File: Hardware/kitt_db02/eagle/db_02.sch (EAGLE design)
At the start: 30 parts, among them T8.1 TPTP09SQ, T8.2 TPTP09SQ, U8 MCP23017ML, X8.1 CON_HEADER_1X08-SMD

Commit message: finished bill of materials for db02 -> layout needs a bit more work on the connector,    which now feature gnd and v+
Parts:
- added J1: FTS-109-01-L-DV, kitt.con:FTS-109-01-L-DV
- renumbered U8 to U8.0
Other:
- note added: "remove"
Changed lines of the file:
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@@
 </classes>
 <parts>
-<part name="U8" library="microchip" deviceset="MCP23017" device="ML" value="MCP23017ML"/>
+<part name="U8.0" library="microchip" deviceset="MCP23017" device="ML" value="MCP23017ML"/>
 <part name="D8.0" library="led" deviceset="LED" device="CHIPLED_1206"/>
 <part name="D8.1" library="led" deviceset="LED" device="CHIPLED_1206"/>
@@
 <part name="GND4" library="supply1" deviceset="GND" device=""/>
 <part name="P+6" library="supply1" deviceset="V+" device=""/>
+<part name="J1" library="kitt.con" deviceset="FTS-109-01-L-DV" device=""/>
 </parts>
 <sheets>
 <sheet>
 <plain>
+<text x="139.7" y="27.94" size="6.4516" layer="98" rot="R180">remove</text>
 </plain>
 <instances>
-<instance part="U8" gate="G$1" x="27.94" y="35.56"/>
+<instance part="U8.0" gate="G$1" x="27.94" y="35.56"/>
 <instance part="D8.0" gate="G$1" x="50.8" y="66.04" rot="MR0"/>
 <instance part="D8.1" gate="G$1" x="60.96" y="66.04" rot="MR0"/>
@@
 <instance part="GND4" gate="1" x="15.24" y="81.28"/>
 <instance part="P+6" gate="1" x="15.24" y="114.3"/>
+<instance part="J1" gate="A" x="149.86" y="25.4"/>
 </instances>
 <busses>
@@
 <net name="N$1" class="0">
 <segment>
-<pinref part="U8" gate="G$1" pin="GPA0"/>
+<pinref part="U8.0" gate="G$1" pin="GPA0"/>
 <pinref part="D8.0" gate="G$1" pin="C"/>
 <wire x1="40.64" y1="55.88" x2="50.8" y2="55.88" width="0.1524" layer="91"/>
@@
 <net name="N$2" class="0">
 <segment>
-<pinref part="U8" gate="G$1" pin="GPA1"/>
+<pinref part="U8.0" gate="G$1" pin="GPA1"/>
 <pinref part="D8.1" gate="G$1" pin="C"/>
 <wire x1="40.64" y1="53.34" x2="60.96" y2="53.34" width="0.1524" layer="91"/>
@@
 <net name="N$3" class="0">
 <segment>
-<pinref part="U8" gate="G$1" pin="GPA2"/>
+<pinref part="U8.0" gate="G$1" pin="GPA2"/>
 <pinref part="D8.2" gate="G$1" pin="C"/>
 <wire x1="40.64" y1="50.8" x2="71.12" y2="50.8" width="0.1524" layer="91"/>
@@
 <net name="N$4" class="0">
 <segment>
-<pinref part="U8" gate="G$1" pin="GPA3"/>
+<pinref part="U8.0" gate="G$1" pin="GPA3"/>
 <pinref part="D8.3" gate="G$1" pin="C"/>
 <wire x1="40.64" y1="48.26" x2="81.28" y2="48.26" width="0.1524" layer="91"/>
@@
 <net name="N$5" class="0">
 <segment>
-<pinref part="U8" gate="G$1" pin="GPA4"/>
+<pinref part="U8.0" gate="G$1" pin="GPA4"/>
 <pinref part="D8.4" gate="G$1" pin="C"/>
 <wire x1="40.64" y1="45.72" x2="91.44" y2="45.72" width="0.1524" layer="91"/>
@@
 <net name="N$6" class="0">
 <segment>
-<pinref part="U8" gate="G$1" pin="GPA5"/>
+<pinref part="U8.0" gate="G$1" pin="GPA5"/>
 <pinref part="D8.5" gate="G$1" pin="C"/>
 <wire x1="40.64" y1="43.18" x2="101.6" y2="43.18" width="0.1524" layer="91"/>
@@
 <net name="N$7" class="0">
 <segment>
-<pinref part="U8" gate="G$1" pin="GPA6"/>
+<pinref part="U8.0" gate="G$1" pin="GPA6"/>
 <pinref part="D8.6" gate="G$1" pin="C"/>
 <wire x1="40.64" y1="40.64" x2="111.76" y2="40.64" width="0.1524" layer="91"/>
@@
 <net name="N$8" class="0">
 <segment>
-<pinref part="U8" gate="G$1" pin="GPA7"/>
+<pinref part="U8.0" gate="G$1" pin="GPA7"/>
 <pinref part="D8.7" gate="G$1" pin="C"/>
 <wire x1="40.64" y1="38.1" x2="121.92" y2="38.1" width="0.1524" layer="91"/>
@@
 <segment>
 <pinref part="P+1" gate="1" pin="V+"/>
-<pinref part="U8" gate="G$1" pin="VDD"/>
+<pinref part="U8.0" gate="G$1" pin="VDD"/>
 <wire x1="12.7" y1="58.42" x2="12.7" y2="55.88" width="0.1524" layer="91"/>
 <wire x1="12.7" y1="55.88" x2="15.24" y2="55.88" width="0.1524" layer="91"/>
@@
 <segment>
 <pinref part="P+5" gate="1" pin="V+"/>
-<pinref part="U8" gate="G$1" pin="!RESET"/>
+<pinref part="U8.0" gate="G$1" pin="!RESET"/>
 <wire x1="5.08" y1="58.42" x2="5.08" y2="50.8" width="0.1524" layer="91"/>
 <wire x1="5.08" y1="50.8" x2="15.24" y2="50.8" width="0.1524" layer="91"/>
@@
 <segment>
 <pinref part="GND2" gate="1" pin="GND"/>
-<pinref part="U8" gate="G$1" pin="VSS"/>
+<pinref part="U8.0" gate="G$1" pin="VSS"/>
 <wire x1="10.16" y1="10.16" x2="10.16" y2="15.24" width="0.1524" layer="91"/>
 <wire x1="10.16" y1="15.24" x2="15.24" y2="15.24" width="0.1524" layer="91"/>
@@
 <wire x1="15.24" y1="33.02" x2="5.08" y2="33.02" width="0.1524" layer="91"/>
 <label x="5.08" y="33.02" size="1.27" layer="95" rot="R180" xref="yes"/>
-<pinref part="U8" gate="G$1" pin="SCL"/>
+<pinref part="U8.0" gate="G$1" pin="SCL"/>
 </segment>
 <segment>
@@
 <wire x1="15.24" y1="30.48" x2="5.08" y2="30.48" width="0.1524" layer="91"/>
 <label x="5.08" y="30.48" size="1.27" layer="95" rot="R180" xref="yes"/>
-<pinref part="U8" gate="G$1" pin="SDA"/>
+<pinref part="U8.0" gate="G$1" pin="SDA"/>
 </segment>
 <segment>
@@
 <pinref part="R8.11" gate="G$1" pin="2"/>
 <wire x1="-15.24" y1="30.48" x2="-15.24" y2="25.4" width="0.1524" layer="91"/>
-<pinref part="U8" gate="G$1" pin="A0"/>
+<pinref part="U8.0" gate="G$1" pin="A0"/>
 <wire x1="-15.24" y1="25.4" x2="-15.24" y2="17.78" width="0.1524" layer="91"/>
 <wire x1="15.24" y1="25.4" x2="-15.24" y2="25.4" width="0.1524" layer="91"/>
@@
 <pinref part="R8.12" gate="G$1" pin="2"/>
 <wire x1="-25.4" y1="30.48" x2="-25.4" y2="22.86" width="0.1524" layer="91"/>
-<pinref part="U8" gate="G$1" pin="A1"/>
+<pinref part="U8.0" gate="G$1" pin="A1"/>
 <wire x1="-25.4" y1="22.86" x2="-25.4" y2="17.78" width="0.1524" layer="91"/>
 <wire x1="15.24" y1="22.86" x2="-25.4" y2="22.86" width="0.1524" layer="91"/>
@@
 <pinref part="R8.13" gate="G$1" pin="2"/>
 <wire x1="-35.56" y1="30.48" x2="-35.56" y2="20.32" width="0.1524" layer="91"/>
-<pinref part="U8" gate="G$1" pin="A2"/>
+<pinref part="U8.0" gate="G$1" pin="A2"/>
 <wire x1="-35.56" y1="20.32" x2="-35.56" y2="17.78" width="0.1524" layer="91"/>
 <wire x1="15.24" y1="20.32" x2="-35.56" y2="20.32" width="0.1524" layer="91"/>
@@
 <net name="GPB0" class="0">
 <segment>
-<pinref part="U8" gate="G$1" pin="GPB0"/>
+<pinref part="U8.0" gate="G$1" pin="GPB0"/>
 <wire x1="48.26" y1="33.02" x2="40.64" y2="33.02" width="0.1524" layer="91"/>
 <label x="43.18" y="33.02" size="1.27" layer="95"/>
@@
 <net name="GPB1" class="0">
 <segment>
-<pinref part="U8" gate="G$1" pin="GPB1"/>
+<pinref part="U8.0" gate="G$1" pin="GPB1"/>
 <wire x1="40.64" y1="30.48" x2="48.26" y2="30.48" width="0.1524" layer="91"/>
 <label x="43.18" y="30.48" size="1.27" layer="95"/>
@@
 </segment>
 <segment>
-<pinref part="U8" gate="G$1" pin="GPB2"/>
+<pinref part="U8.0" gate="G$1" pin="GPB2"/>
 <wire x1="40.64" y1="27.94" x2="48.26" y2="27.94" width="0.1524" layer="91"/>
 <label x="43.18" y="27.94" size="1.27" layer="95"/>
@@
 <net name="GPB3" class="0">
 <segment>
-<pinref part="U8" gate="G$1" pin="GPB3"/>
+<pinref part="U8.0" gate="G$1" pin="GPB3"/>
 <wire x1="48.26" y1="25.4" x2="40.64" y2="25.4" width="0.1524" layer="91"/>
 <label x="43.18" y="25.4" size="1.27" layer="95"/>
@@
 <net name="GPB4" class="0">
 <segment>
-<pinref part="U8" gate="G$1" pin="GPB4"/>
+<pinref part="U8.0" gate="G$1" pin="GPB4"/>
 <wire x1="40.64" y1="22.86" x2="48.26" y2="22.86" width="0.1524" layer="91"/>
 <label x="43.18" y="22.86" size="1.27" layer="95"/>
@@
 <net name="GPB5" class="0">
 <segment>
-<pinref part="U8" gate="G$1" pin="GPB5"/>
+<pinref part="U8.0" gate="G$1" pin="GPB5"/>
 <wire x1="40.64" y1="20.32" x2="48.26" y2="20.32" width="0.1524" layer="91"/>
 <label x="43.18" y="20.32" size="1.27" layer="95"/>
@@
 </segment>
 <segment>
-<pinref part="U8" gate="G$1" pin="GPB6"/>
+<pinref part="U8.0" gate="G$1" pin="GPB6"/>
 <wire x1="40.64" y1="17.78" x2="48.26" y2="17.78" width="0.1524" layer="91"/>
 <label x="43.18" y="17.78" size="1.27" layer="95"/>
@@
 </segment>
 <segment>
-<pinref part="U8" gate="G$1" pin="GPB7"/>
+<pinref part="U8.0" gate="G$1" pin="GPB7"/>
 <wire x1="40.64" y1="15.24" x2="48.26" y2="15.24" width="0.1524" layer="91"/>
 <label x="43.18" y="15.24" size="1.27" layer="95"/>
@@
 <segment>
 <pinref part="T8.1" gate="G$1" pin="TP"/>
-<pinref part="U8" gate="G$1" pin="INTA"/>
+<pinref part="U8.0" gate="G$1" pin="INTA"/>
 <wire x1="2.54" y1="45.72" x2="15.24" y2="45.72" width="0.1524" layer="91"/>
 </segment>
@@
 <segment>
 <pinref part="T8.2" gate="G$1" pin="TP"/>
-<pinref part="U8" gate="G$1" pin="INTB"/>
+<pinref part="U8.0" gate="G$1" pin="INTB"/>
 <wire x1="-2.54" y1="43.18" x2="15.24" y2="43.18" width="0.1524" layer="91"/>
 </segment>

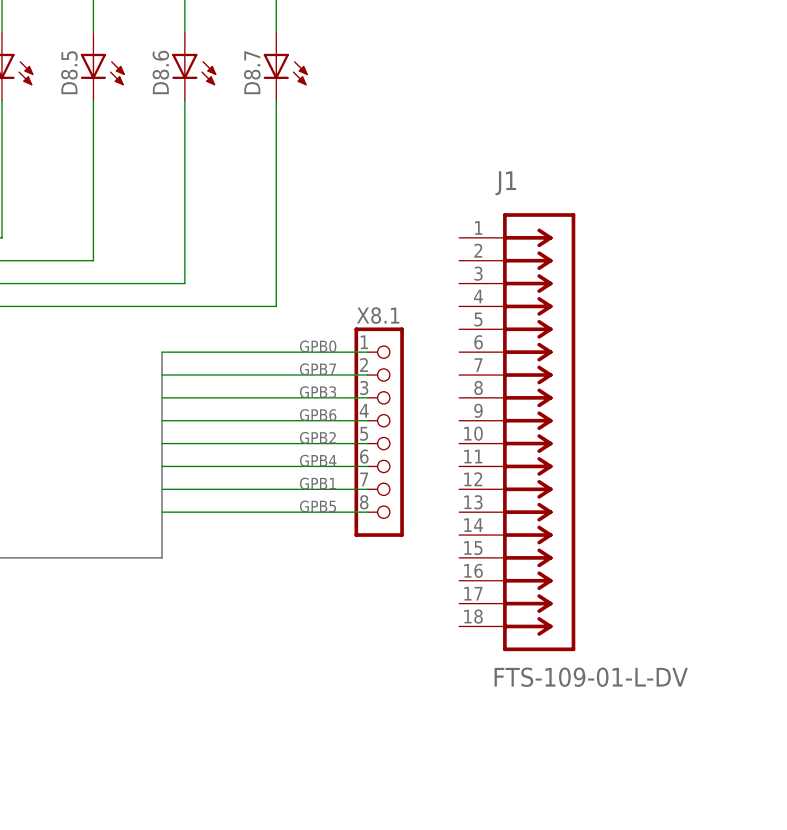
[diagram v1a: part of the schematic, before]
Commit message: snapshot of db02 board layout : this is going nowhere edition -> reverting back to previous version
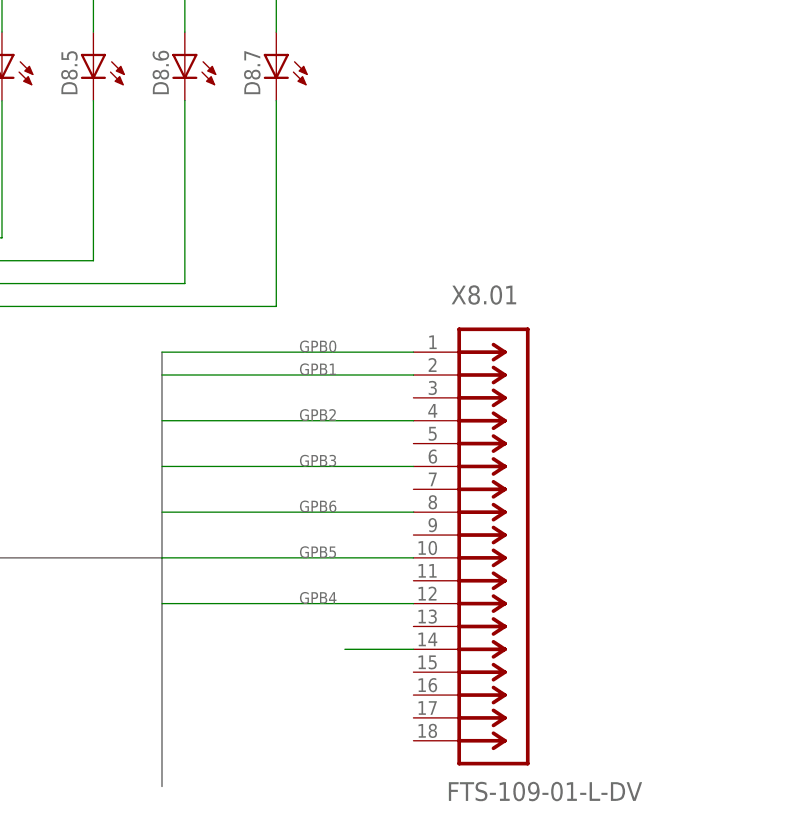
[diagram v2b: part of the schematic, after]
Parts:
- removed J1: FTS-109-01-L-DV, kitt.con:FTS-109-01-L-DV
- removed X8.1: CON_HEADER_1X08-SMD, dp_devices:CON_HEADER_1X08-SMD
- added X8.01: FTS-109-01-L-DV, kitt.con:FTS-109-01-L-DV
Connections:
- net GPB0: now also X8.01.1; no longer X8.1.1
- net GPB1: now also X8.01.2; no longer X8.1.7
- net GPB2: now also X8.01.4; no longer X8.1.5
- net GPB3: now also X8.01.6; no longer X8.1.3
- net GPB4: now also X8.01.12; no longer X8.1.6
- net GPB5: now also X8.01.10; no longer X8.1.8
- net GPB6: now also X8.01.8; no longer X8.1.4
- net GPB7: now also X8.01.14; no longer X8.1.2
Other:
- note removed: "remove"
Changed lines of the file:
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@@
 <part name="GND3" library="supply1" deviceset="GND" device=""/>
 <part name="P+5" library="supply1" deviceset="V+" device=""/>
-<part name="X8.1" library="dp_devices" deviceset="CON_HEADER_1X08" device="-SMD"/>
 <part name="T8.1" library="testpad" deviceset="TP" device="TP09SQ" value="TPTP09SQ"/>
 <part name="T8.2" library="testpad" deviceset="TP" device="TP09SQ" value="TPTP09SQ"/>
@@
 <part name="GND4" library="supply1" deviceset="GND" device=""/>
 <part name="P+6" library="supply1" deviceset="V+" device=""/>
-<part name="J1" library="kitt.con" deviceset="FTS-109-01-L-DV" device=""/>
+<part name="X8.01" library="kitt.con" deviceset="FTS-109-01-L-DV" device=""/>
 </parts>
 <sheets>
 <sheet>
 <plain>
-<text x="139.7" y="27.94" size="6.4516" layer="98" rot="R180">remove</text>
 </plain>
 <instances>
@@
 <instance part="GND3" gate="1" x="-25.4" y="0"/>
 <instance part="P+5" gate="1" x="5.08" y="60.96"/>
-<instance part="X8.1" gate="J" x="132.08" y="25.4"/>
 <instance part="T8.1" gate="G$1" x="0" y="45.72" rot="R90"/>
 <instance part="T8.2" gate="G$1" x="-5.08" y="43.18" rot="R90"/>
@@
 <instance part="GND4" gate="1" x="15.24" y="81.28"/>
 <instance part="P+6" gate="1" x="15.24" y="114.3"/>
-<instance part="J1" gate="A" x="149.86" y="25.4"/>
+<instance part="X8.01" gate="A" x="144.78" y="12.7"/>
 </instances>
 <busses>
@@
 <wire x1="48.26" y1="10.16" x2="109.22" y2="10.16" width="0.762" layer="92"/>
 <wire x1="109.22" y1="10.16" x2="109.22" y2="33.02" width="0.762" layer="92"/>
+<wire x1="109.22" y1="10.16" x2="109.22" y2="-15.24" width="0.762" layer="92"/>
 </segment>
 </bus>
@@
 </segment>
 <segment>
-<pinref part="X8.1" gate="J" pin="1"/>
-<wire x1="132.08" y1="33.02" x2="109.22" y2="33.02" width="0.1524" layer="91"/>
 <label x="124.46" y="33.02" size="1.27" layer="95"/>
+<pinref part="X8.01" gate="A" pin="1"/>
+<wire x1="137.16" y1="33.02" x2="109.22" y2="33.02" width="0.1524" layer="91"/>
 </segment>
 </net>
@@
 </segment>
 <segment>
-<pinref part="X8.1" gate="J" pin="7"/>
-<wire x1="109.22" y1="17.78" x2="132.08" y2="17.78" width="0.1524" layer="91"/>
-<label x="124.46" y="17.78" size="1.27" layer="95"/>
+<pinref part="X8.01" gate="A" pin="2"/>
+<wire x1="109.22" y1="30.48" x2="137.16" y2="30.48" width="0.1524" layer="91"/>
+<label x="124.46" y="30.48" size="1.27" layer="95"/>
 </segment>
 </net>
 <net name="GPB2" class="0">
-<segment>
-<pinref part="X8.1" gate="J" pin="5"/>
-<wire x1="109.22" y1="22.86" x2="132.08" y2="22.86" width="0.1524" layer="91"/>
-<label x="124.46" y="22.86" size="1.27" layer="95"/>
-</segment>
 <segment>
 <pinref part="U8.0" gate="G$1" pin="GPB2"/>
@@
 <label x="43.18" y="27.94" size="1.27" layer="95"/>
 </segment>
+<segment>
+<wire x1="109.22" y1="25.4" x2="137.16" y2="25.4" width="0.1524" layer="91"/>
+<label x="124.46" y="25.4" size="1.27" layer="95"/>
+<pinref part="X8.01" gate="A" pin="4"/>
+</segment>
 </net>
 <net name="GPB3" class="0">
@@
 </segment>
 <segment>
-<pinref part="X8.1" gate="J" pin="3"/>
-<wire x1="132.08" y1="27.94" x2="109.22" y2="27.94" width="0.1524" layer="91"/>
-<label x="124.46" y="27.94" size="1.27" layer="95"/>
+<pinref part="X8.01" gate="A" pin="6"/>
+<wire x1="109.22" y1="20.32" x2="137.16" y2="20.32" width="0.1524" layer="91"/>
+<label x="124.46" y="20.32" size="1.27" layer="95"/>
 </segment>
 </net>
@@
 </segment>
 <segment>
-<pinref part="X8.1" gate="J" pin="6"/>
-<wire x1="109.22" y1="20.32" x2="132.08" y2="20.32" width="0.1524" layer="91"/>
-<label x="124.46" y="20.32" size="1.27" layer="95"/>
+<wire x1="109.22" y1="5.08" x2="137.16" y2="5.08" width="0.1524" layer="91"/>
+<label x="124.46" y="5.08" size="1.27" layer="95"/>
+<pinref part="X8.01" gate="A" pin="12"/>
 </segment>
 </net>
@@
 </segment>
 <segment>
-<pinref part="X8.1" gate="J" pin="8"/>
-<wire x1="109.22" y1="15.24" x2="132.08" y2="15.24" width="0.1524" layer="91"/>
-<label x="124.46" y="15.24" size="1.27" layer="95"/>
+<wire x1="109.22" y1="10.16" x2="137.16" y2="10.16" width="0.1524" layer="91"/>
+<label x="124.46" y="10.16" size="1.27" layer="95"/>
+<pinref part="X8.01" gate="A" pin="10"/>
 </segment>
 </net>
 <net name="GPB6" class="0">
-<segment>
-<pinref part="X8.1" gate="J" pin="4"/>
-<wire x1="109.22" y1="25.4" x2="132.08" y2="25.4" width="0.1524" layer="91"/>
-<label x="124.46" y="25.4" size="1.27" layer="95"/>
-</segment>
 <segment>
 <pinref part="U8.0" gate="G$1" pin="GPB6"/>
@@
 <label x="43.18" y="17.78" size="1.27" layer="95"/>
 </segment>
+<segment>
+<wire x1="109.22" y1="15.24" x2="137.16" y2="15.24" width="0.1524" layer="91"/>
+<label x="124.46" y="15.24" size="1.27" layer="95"/>
+<pinref part="X8.01" gate="A" pin="8"/>
+</segment>
 </net>
 <net name="GPB7" class="0">
-<segment>
-<pinref part="X8.1" gate="J" pin="2"/>
-<wire x1="109.22" y1="30.48" x2="132.08" y2="30.48" width="0.1524" layer="91"/>
-<label x="124.46" y="30.48" size="1.27" layer="95"/>
-</segment>
 <segment>
 <pinref part="U8.0" gate="G$1" pin="GPB7"/>
@@
 <label x="43.18" y="15.24" size="1.27" layer="95"/>
 </segment>
-</net>
+<segment>
+<wire x1="129.54" y1="0" x2="137.16" y2="0" width="0.1524" layer="91"/>
+<pinref part="X8.01" gate="A" pin="14"/>
+</segment>
+</net>

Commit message: restored db02 board layout from commit acb6896f0427ddee216c2485e595b1a3f3064529
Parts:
- removed X8.01: FTS-109-01-L-DV, kitt.con:FTS-109-01-L-DV
- added X8.1: CON_HEADER_1X08-SMD, dp_devices:CON_HEADER_1X08-SMD
- renumbered U8.0 to U8
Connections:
- net GPB0: now also X8.1.1; no longer X8.01.1
- net GPB1: now also X8.1.7; no longer X8.01.2
- net GPB2: now also X8.1.5; no longer X8.01.4
- net GPB3: now also X8.1.3; no longer X8.01.6
- net GPB4: now also X8.1.6; no longer X8.01.12
- net GPB5: now also X8.1.8; no longer X8.01.10
- net GPB6: now also X8.1.4; no longer X8.01.8
- net GPB7: now also X8.1.2; no longer X8.01.14
